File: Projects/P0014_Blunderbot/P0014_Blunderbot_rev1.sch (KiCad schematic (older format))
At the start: 6 parts

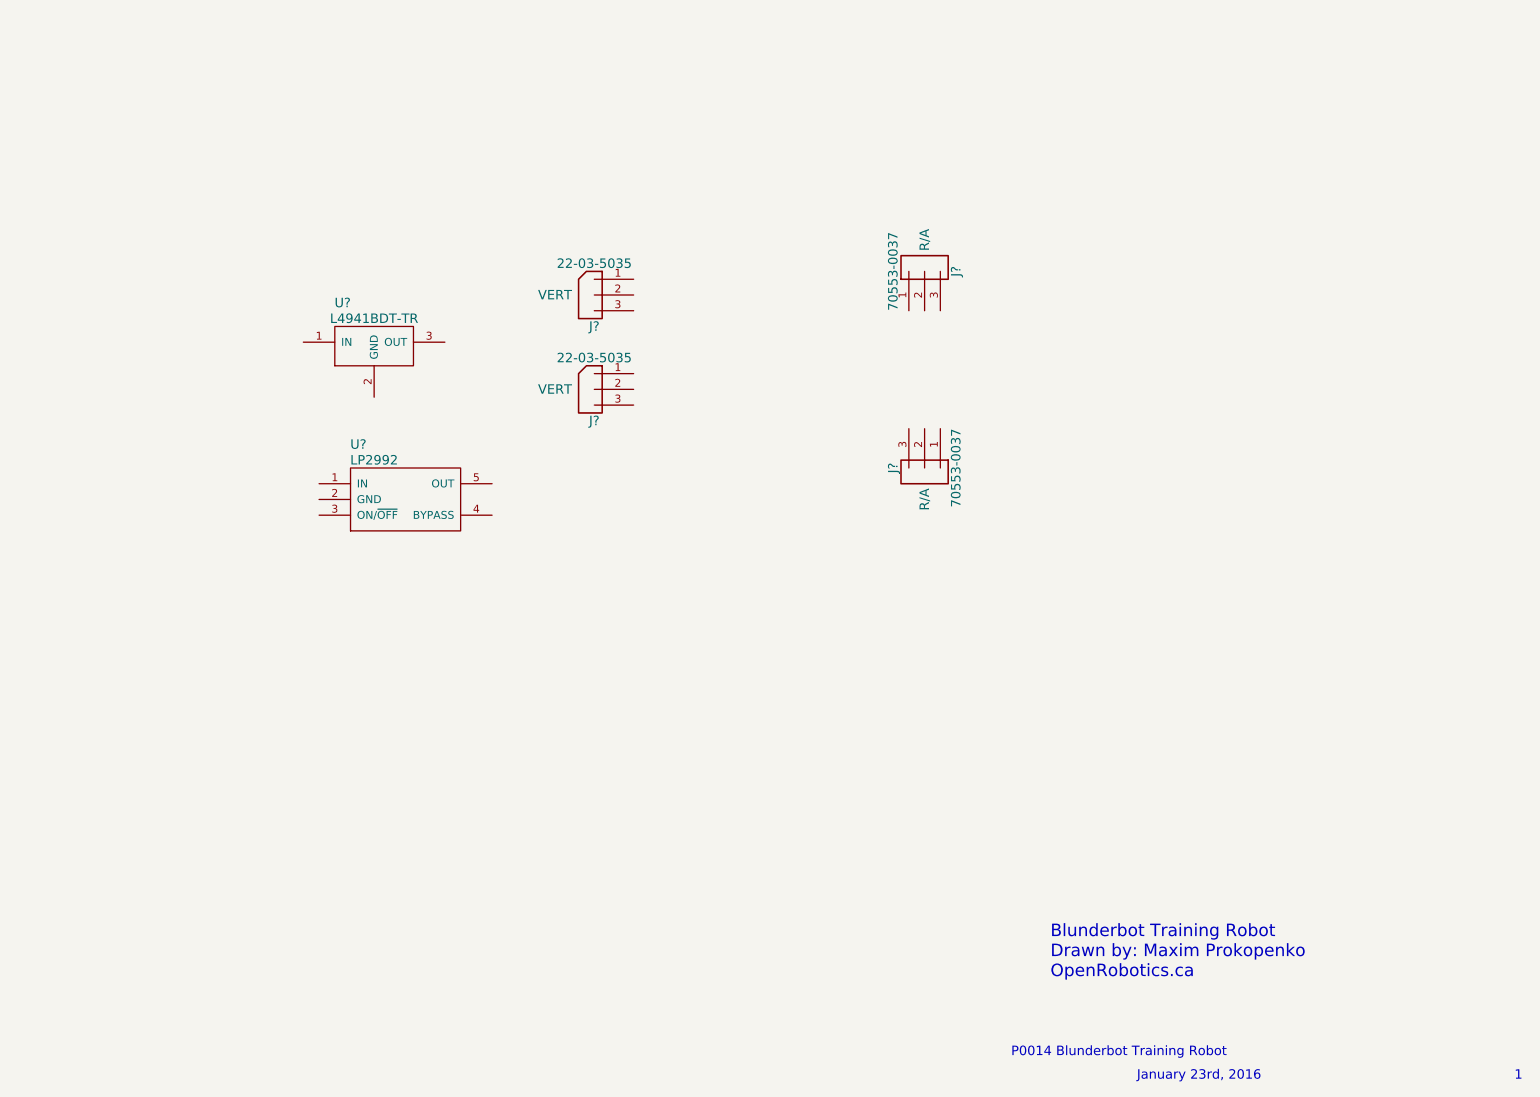
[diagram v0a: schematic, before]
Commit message: First pass at P0014rev1 schematic
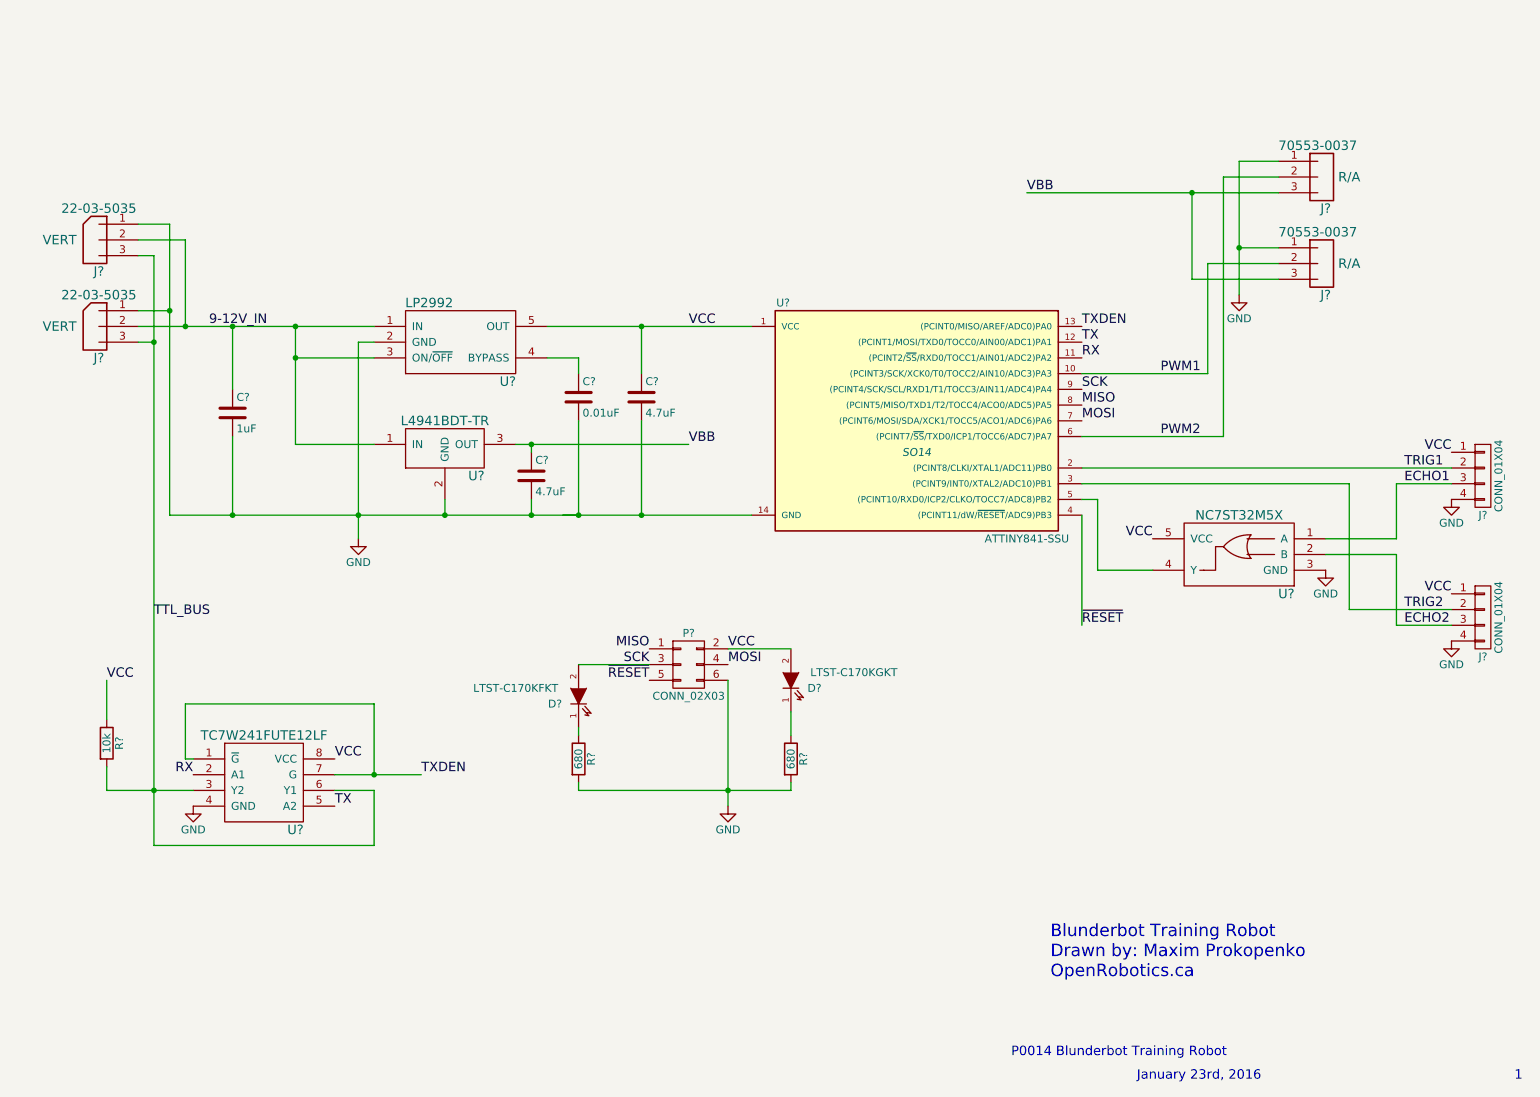
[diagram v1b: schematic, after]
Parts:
- added C?: 1uF, symbol C
- added C? (x2): 4.7uF, symbol C
- added C?: 0.01uF, symbol C
- added D?: LTST-C170KGKT, symbol LTST-C170KGKT
- added D?: LTST-C170KFKT, symbol LTST-C170KFKT
- added J? (x2): CONN_01X04, symbol CONN_01X04
- added P?: CONN_02X03, symbol CONN_02X03
- added R? (x2): 680, symbol R
- added R?: 10k, symbol R
- added U?: ATTINY841-SSU, SO14, symbol ATTINY841-SSU
- added U?: TC7W241FUTE12LF, symbol TC7W241FUTE12LF
- added U?: NC7ST32M5X, symbol NC7ST32
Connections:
- net GND: now reaches J?.1
- net GND: now also J?.1, J?.1, J?.1, U?.2 (GND), U?.2 (GND), C?.2, C?.2, C?.2, C?.2, J?.4 (P4), J?.4 (P4), P?.6 (P6), R?.2, R?.2, U?.14 (GND), U?.3 (GND), U?.4 (GND)
- net PWM1: now reaches J?.2
- net PWM1: now also U?.10 ((PCINT3/SCK/XCK0/T0/TOCC2/AIN10/ADC3)PA3)
- net VBB: now reaches J?.3
- net VBB: now also J?.3, U?.3 (OUT), C?.1
- net PWM2: now reaches J?.2
- net PWM2: now also U?.6 ((PCINT7/~SS~/TXD0/ICP1/TOCC6/ADC7)PA7)
- net 9-12V_IN: now reaches J?.2
- net 9-12V_IN: now also J?.2, U?.1 (IN), U?.1 (IN), U?.3 (ON/~OFF), C?.1
- net TTL_BUS: now reaches J?.3
- net TTL_BUS: now also J?.3, R?.2, U?.3 (Y2), U?.6 (Y1)
- net at U?.4 (BYPASS): now also C?.1
- net VCC: now reaches U?.5 (OUT)
- net VCC: now also C?.1, D?.2 (A), J?.1 (P1), J?.1 (P1), P?.2 (P2), R?.1, U?.1 (VCC), U?.5 (VCC), U?.8 (VCC)
- new net: U?.4 (Y), U?.5 ((PCINT10/RXD0/ICP2/CLKO/TOCC7/ADC8)PB2)
- new net: D?.1 (K), R?.1 (x2)
- new net ECHO1: J?.3 (P3), U?.1 (A)
- new net ECHO2: J?.3 (P3), U?.2 (B)
- new net MISO: P?.1 (P1), U?.8 ((PCINT5/MISO/TXD1/T2/TOCC4/ACO0/ADC5)PA5)
- new net MOSI: P?.4 (P4), U?.7 ((PCINT6/MOSI/SDA/XCK1/TOCC5/ACO1/ADC6)PA6)
- new net RX: U?.11 ((PCINT2/~SS~/RXD0/TOCC1/AIN01/ADC2)PA2), U?.2 (A1)
- new net SCK: D?.2 (A), P?.3 (P3), U?.9 ((PCINT4/SCK/SCL/RXD1/T1/TOCC3/AIN11/ADC4)PA4)
- new net TRIG1: J?.2 (P2), U?.2 ((PCINT8/CLKI/XTAL1/ADC11)PB0)
- new net TRIG2: J?.2 (P2), U?.3 ((PCINT9/INT0/XTAL2/ADC10)PB1)
- new net TX: U?.12 ((PCINT1/MOSI/TXD0/TOCC0/AIN00/ADC1)PA1), U?.5 (A2)
- new net TXDEN: U?.1 (~G), U?.13 ((PCINT0/MISO/AREF/ADC0)PA0), U?.7 (G)
- new net ~RESET: P?.5 (P5), U?.4 ((PCINT11/dW/~RESET~/ADC9)PB3)
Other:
- moved on the sheet: J?, U?

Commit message: Started power distribution unit
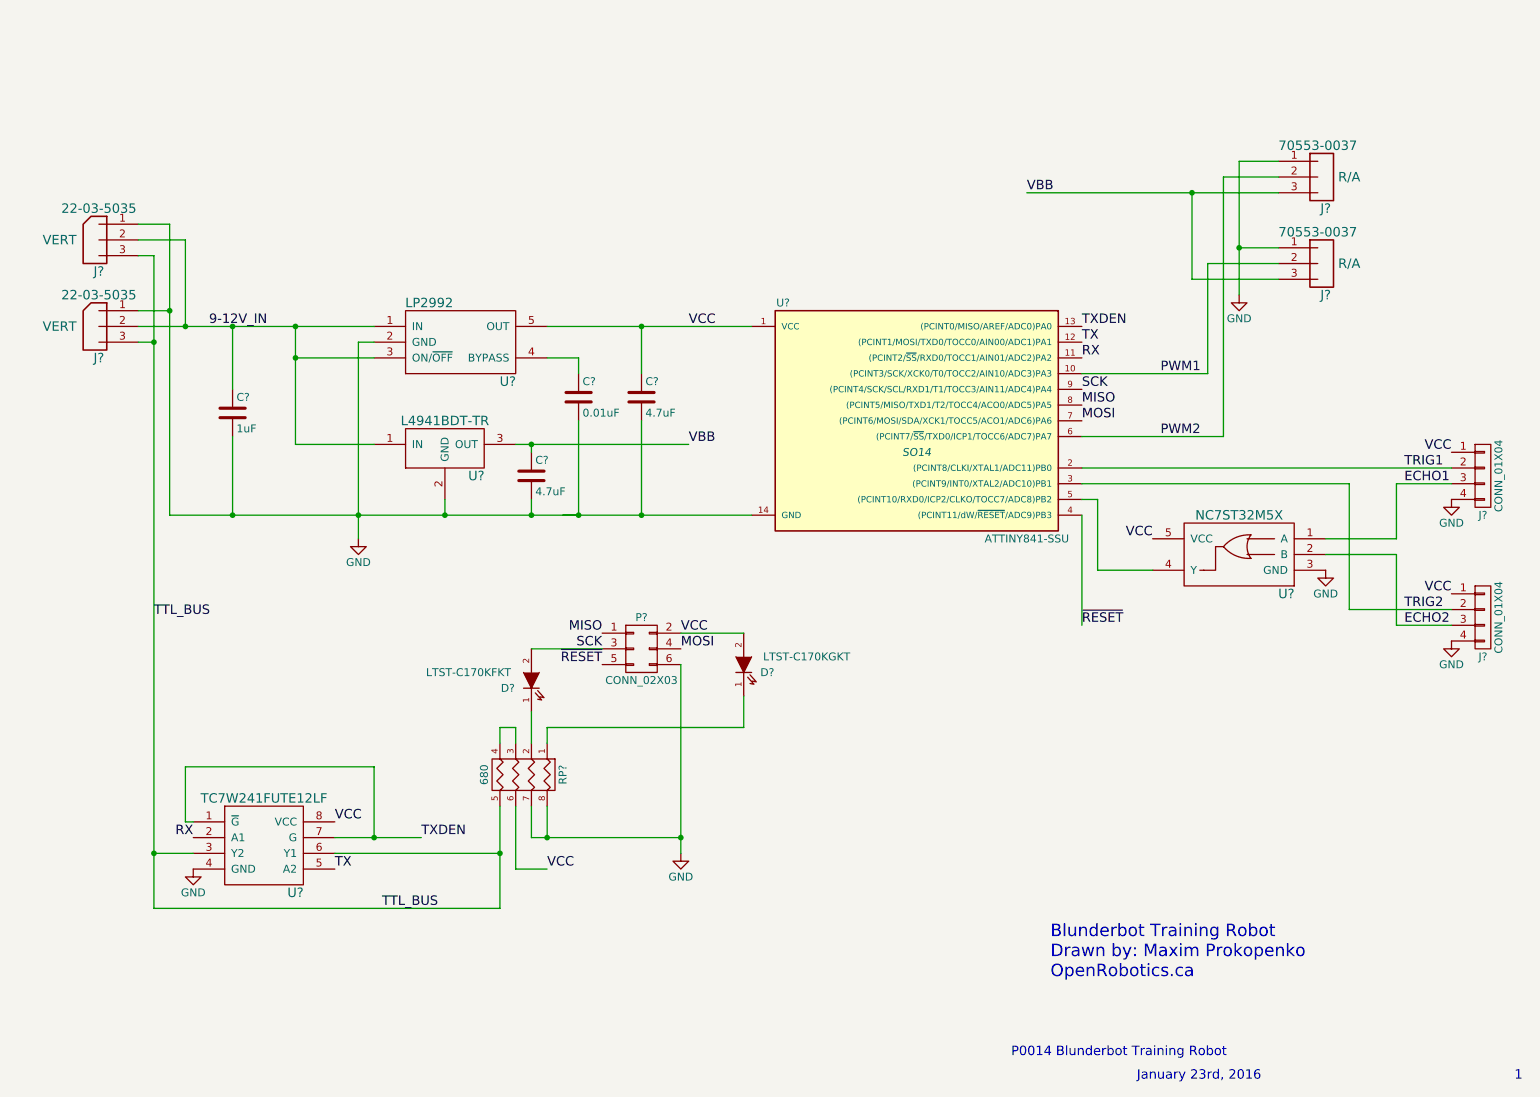
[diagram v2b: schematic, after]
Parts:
- removed R? (x2): 680, symbol R
- removed R?: 10k, symbol R
- added RP?: 680, symbol R_PACK4
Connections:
- net GND: now also RP?.7 (R2), RP?.8 (R1)
- net TTL_BUS: now also RP?.5 (R4)
- net VCC: now also RP?.6 (R3)
- net at D?.1 (K): now also RP?.1 (P1)
- net at D?.1 (K): now also RP?.2 (P2)
- new net: RP?.3 (P3), RP?.4 (P4)
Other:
- moved on the sheet: D?, P?, U?

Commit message: Layout pt 1
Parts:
- removed U?: LP2992, symbol LP2992
- removed U?: L4941BDT-TR, symbol L4941BDT-TR
- removed U?: NC7ST32M5X, symbol NC7ST32
- added C3: 470pF, Capacitors_SMD:C_0805_HandSoldering, symbol C
- added U2, U3: MIC5219-5.0YM5-TR, TO_SOT_Packages_SMD:SOT-23-5, symbol MIC5219-5.0YM5-TR
- C1, C4, C5: renamed from C?; footprint (none) -> Capacitors_SMD:C_0805_HandSoldering
- C2: renamed from C?; value 0.01uF -> 470pF; footprint (none) -> Capacitors_SMD:C_0805_HandSoldering
- D1, D2: renamed from D?; footprint (none) -> LEDs:LED_0805
- J1, J2: renamed from J?; footprint (none) -> Pin_Headers:Pin_Header_Straight_1x03
- J3, J4: renamed from J?; footprint (none) -> Pin_Headers:Pin_Header_Angled_1x03
- J5, J6: renamed from J?; footprint (none) -> Pin_Headers:Pin_Header_Straight_1x04
- P1: renamed from P?; footprint (none) -> Pin_Headers:Pin_Header_Straight_2x03
- RP1: renamed from RP?; footprint (none) -> Resistors_SMD:R_Array_Convex_4x1206
- U1: renamed from U?; footprint (none) -> Housings_SSOP:MSOP-8_3x3mm_Pitch0.65mm
- U4: renamed from U?; footprint SO14 -> SMD_Packages:SOIC-14_N
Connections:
- net TX is gone; now on net PWM1: U1.5 (A2), U4.12 ((PCINT1/MOSI/TXD0/TOCC0/AIN00/ADC1)PA1)
- net 9-12V_IN: now also U2.1 (IN), U2.3 (ON/~OFF), U3.1 (IN)
- net ECHO1: now also J5.2 (P2), U4.2 ((PCINT8/CLKI/XTAL1/ADC11)PB0); no longer J5.3 (P3)
- net ECHO2: now also J6.2 (P2), U4.5 ((PCINT10/RXD0/ICP2/CLKO/TOCC7/ADC8)PB2); no longer J6.3 (P3)
- net GND: now also J5.1 (P1), J6.1 (P1), C3.2, U2.2 (GND), U3.2 (GND); no longer J5.4 (P4), J6.4 (P4)
- net MISO: now also J3.2
- net PWM1: no longer U4.10 ((PCINT3/SCK/XCK0/T0/TOCC2/AIN10/ADC3)PA3)
- net TRIG1: now also J5.3 (P3), U4.6 ((PCINT7/~SS~/TXD0/ICP1/TOCC6/ADC7)PA7); no longer J5.2 (P2), U4.2 ((PCINT8/CLKI/XTAL1/ADC11)PB0)
- net TRIG2: now also J6.3 (P3); no longer J6.2 (P2)
- net VBB: now also U3.5 (OUT)
- net VCC: now also J5.4 (P4), J6.4 (P4), U2.5 (OUT); no longer J5.1 (P1), J6.1 (P1)
- net at C2.1: now also U3.4 (BYPASS)
- removed net PWM2: J3.2, U4.6 ((PCINT7/~SS~/TXD0/ICP1/TOCC6/ADC7)PA7)
- new net: C3.1, U2.4 (BYPASS)
- new net SERVO_EN: U3.3 (ON/~OFF), U4.10 ((PCINT3/SCK/XCK0/T0/TOCC2/AIN10/ADC3)PA3)
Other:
- moved on the sheet: C1, C2, C4, C5, D1, D2, J1, J2, J5, J6, P1, RP1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

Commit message: layout nearly done
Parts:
- added S1: MHSS1105, Pin_Headers:Pin_Header_Straight_1x03, symbol MHSS1105
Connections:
- net SERVO_EN: now also U4.13 ((PCINT0/MISO/AREF/ADC0)PA0); no longer U4.10 ((PCINT3/SCK/XCK0/T0/TOCC2/AIN10/ADC3)PA3)
- net TXDEN: now also U4.10 ((PCINT3/SCK/XCK0/T0/TOCC2/AIN10/ADC3)PA3); no longer U4.13 ((PCINT0/MISO/AREF/ADC0)PA0)
- net 9-12V_IN renamed 9-10V_IN
- net 9-10V_IN: now also S1.2; no longer U2.3 (ON/~OFF)
- net MISO renamed MISO/PWM1
- net MISO/PWM1: now also J4.2; no longer J3.2
- net MOSI renamed MOSI/PWM2
- net MOSI/PWM2: now also J3.2
- net PWM1 renamed TX
- net TX: no longer J4.2
- new net: S1.3, U2.3 (ON/~OFF)
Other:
- moved on the sheet: D2
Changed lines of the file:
@@
 	1950 2300 1950 2850
 Connection ~ 1950 2850
-Text Label 2100 2850 0    60   ~ 0
-9-12V_IN
+Text Label 1950 2300 0    60   ~ 0
+9-10V_IN
 Wire Wire Line
 	1650 2400 1750 2400
@@
 Wire Wire Line
 	1750 2950 1650 2950
-Wire Wire Line
-	3150 3050 2650 3050
 Wire Wire Line
 	2650 2850 2650 3450
@@
 Wire Wire Line
 	2650 3450 3150 3450
-Connection ~ 2650 3050
 Wire Wire Line
 	3150 2950 2850 2950
@@
 Connection ~ 1850 2750
 Wire Wire Line
-	2250 3250 2250 2850
+	2250 2550 2250 3250
 Connection ~ 2250 2850
 Wire Wire Line
@@
 Text Label 7800 4750 0    60   ~ 0
 ~RESET
-Text Label 7800 3350 0    60   ~ 0
-MISO
 Text Label 7800 3450 0    60   ~ 0
-MOSI
+MOSI/PWM2
 Text Label 7800 3250 0    60   ~ 0
 SCK
@@
 RX
 Wire Wire Line
-	8600 2950 8600 2450
-Wire Wire Line
 	8600 2450 9050 2450
-Text Label 8300 2950 0    60   ~ 0
-PWM1
 Wire Wire Line
 	9050 2350 8800 2350
@@
 	1    0    0    -1
 $EndComp
-Text Label 9300 3550 0    60   ~ 0
+Text Label 7800 3550 0    60   ~ 0
 TRIG1
-Text Label 9300 4200 0    60   ~ 0
+Text Label 7800 3850 0    60   ~ 0
 TRIG2
-Text Label 9300 4300 0    60   ~ 0
+Text Label 7800 3950 0    60   ~ 0
 ECHO2
-Text Label 7800 2850 0    60   ~ 0
+Text Label 7800 3150 0    60   ~ 0
 TXDEN
 $Comp
 L LTST-C170KGKT D2
 U 1 1 56A60844
-P 5550 5000
-F 0 "D2" V 5500 4850 50  0000 C CNN
-F 1 "LTST-C170KGKT" V 5600 4600 50  0000 C CNN
-F 2 "LEDs:LED_0805" V 5550 5000 50  0001 C CNN
-F 3 "" H 5550 5000 50  0000 C CNN
-	1    5550 5000
+P 5850 5000
+F 0 "D2" V 5800 4850 50  0000 C CNN
+F 1 "LTST-C170KGKT" V 5900 4600 50  0000 C CNN
+F 2 "LEDs:LED_0805" V 5850 5000 50  0001 C CNN
+F 3 "" H 5850 5000 50  0000 C CNN
+	1    5850 5000
 	0    -1   -1   0
 $EndComp
@@
 $EndComp
 Wire Wire Line
-	5100 4800 5550 4800
+	5100 4800 5850 4800
 Text Label 4600 4800 2    60   ~ 0
-MISO
+MISO/PWM1
 Text Label 4600 4900 2    60   ~ 0
 SCK
@@
 VCC
 Text Label 5100 4900 0    60   ~ 0
-MOSI
-Wire Wire Line
-	5550 5200 5550 5400
+MOSI/PWM2
+Wire Wire Line
+	5850 5200 5850 5400
 Wire Wire Line
 	4150 5300 4150 5500
@@
 	4250 5500 4250 5400
 Wire Wire Line
-	4250 5400 5550 5400
+	4250 5400 5850 5400
 Wire Wire Line
 	4250 5900 4250 6100
@@
 	9050 1900 8950 1900
 Wire Wire Line
-	8950 1900 8950 3350
-Wire Wire Line
-	8950 3350 7800 3350
-Text Label 8300 3350 0    60   ~ 0
-PWM2
-Wire Wire Line
-	8600 2950 7800 2950
+	8950 1900 8950 3450
+Text Label 7800 3350 0    60   ~ 0
+MISO/PWM1
 Wire Wire Line
 	9600 3550 7800 3550
@@
 	8700 3650 8700 3750
 Wire Wire Line
-	8700 3750 7800 3750
-Wire Wire Line
 	7800 3850 8700 3850
 Wire Wire Line
@@
 Wire Wire Line
 	8600 3950 7800 3950
-Text Label 9300 3650 0    60   ~ 0
+Text Label 7800 3750 0    60   ~ 0
 ECHO1
+$Comp
+L MIC5219-5.0YM5-TR U3
+U 1 1 56C97863
+P 3700 3450
+F 0 "U3" H 4000 3100 60  0000 C CNN
+F 1 "MIC5219-5.0YM5-TR" H 3700 3600 60  0000 C CNN
+F 2 "TO_SOT_Packages_SMD:SOT-23-5" H 3700 3450 60  0001 C CNN
+F 3 "" H 3700 3450 60  0000 C CNN
+	1    3700 3450
+	1    0    0    -1
+$EndComp
+Wire Wire Line
+	3150 3550 2950 3550
+Wire Wire Line
+	2950 3550 2950 4050
+Connection ~ 2950 4050
+Text Label 7800 2850 0    60   ~ 0
+SERVO_EN
+Text Label 3050 4500 0    60   ~ 0
+SERVO_EN
+Wire Wire Line
+	3050 4500 3050 3650
+Wire Wire Line
+	3050 3650 3150 3650
+Wire Wire Line
+	4250 3650 4400 3650
+Wire Wire Line
+	4400 3650 4400 3700
+Wire Wire Line
+	4400 4000 4400 4050
+Connection ~ 4400 4050
+$Comp
+L C C3
+U 1 1 56C98142
+P 4700 3250
+F 0 "C3" H 4725 3350 50  0000 L CNN
+F 1 "470pF" H 4725 3150 50  0000 L CNN
+F 2 "Capacitors_SMD:C_0805_HandSoldering" H 4738 3100 50  0001 C CNN
+F 3 "" H 4700 3250 50  0000 C CNN
+	1    4700 3250
+	1    0    0    -1
+$EndComp
+Wire Wire Line
+	4700 3400 4700 4050
+Connection ~ 4700 4050
+Wire Wire Line
+	4700 3050 4700 3100
+Wire Wire Line
+	4250 3450 5000 3450
+Wire Wire Line
+	5000 2000 5000 3700
+Wire Wire Line
+	5000 4000 5000 4050
+Connection ~ 5000 4050
+Connection ~ 5000 3450
 $Comp
 L MIC5219-5.0YM5-TR U2
@@
 	1    0    0    -1
 $EndComp
-$Comp
-L MIC5219-5.0YM5-TR U3
-U 1 1 56C97863
-P 3700 3450
-F 0 "U3" H 4000 3100 60  0000 C CNN
-F 1 "MIC5219-5.0YM5-TR" H 3700 3600 60  0000 C CNN
-F 2 "TO_SOT_Packages_SMD:SOT-23-5" H 3700 3450 60  0001 C CNN
-F 3 "" H 3700 3450 60  0000 C CNN
-	1    3700 3450
-	1    0    0    -1
-$EndComp
-Wire Wire Line
-	3150 3550 2950 3550
-Wire Wire Line
-	2950 3550 2950 4050
-Connection ~ 2950 4050
-Wire Wire Line
-	7800 3150 8300 3150
-Text Label 8300 3150 0    60   ~ 0
-SERVO_EN
-Text Label 3050 4500 0    60   ~ 0
-SERVO_EN
-Wire Wire Line
-	3050 4500 3050 3650
-Wire Wire Line
-	3050 3650 3150 3650
-Wire Wire Line
-	4250 3650 4400 3650
-Wire Wire Line
-	4400 3650 4400 3700
-Wire Wire Line
-	4400 4000 4400 4050
-Connection ~ 4400 4050
-$Comp
-L C C3
-U 1 1 56C98142
-P 4700 3250
-F 0 "C3" H 4725 3350 50  0000 L CNN
-F 1 "470pF" H 4725 3150 50  0000 L CNN
-F 2 "Capacitors_SMD:C_0805_HandSoldering" H 4738 3100 50  0001 C CNN
-F 3 "" H 4700 3250 50  0000 C CNN
-	1    4700 3250
-	1    0    0    -1
-$EndComp
-Wire Wire Line
-	4700 3400 4700 4050
-Connection ~ 4700 4050
-Wire Wire Line
-	4700 3050 4700 3100
-Wire Wire Line
-	4250 3450 5000 3450
-Wire Wire Line
-	5000 2000 5000 3700
-Wire Wire Line
-	5000 4000 5000 4050
-Connection ~ 5000 4050
-Connection ~ 5000 3450
+Wire Wire Line
+	8700 3750 7800 3750
+$Comp
+L MHSS1105 S1
+U 1 1 56C9F259
+P 2750 2550
+F 0 "S1" H 2950 2375 60  0000 C CNN
+F 1 "MHSS1105" H 2750 2775 60  0000 C CNN
+F 2 "Pin_Headers:Pin_Header_Straight_1x03" H 2860 2550 60  0001 C CNN
+F 3 "" H 2860 2550 60  0000 C CNN
+	1    2750 2550
+	1    0    0    -1
+$EndComp
+Wire Wire Line
+	3050 2650 3100 2650
+Wire Wire Line
+	3100 2650 3100 3050
+Wire Wire Line
+	3100 3050 3150 3050
+Wire Wire Line
+	2450 2550 2250 2550
+Wire Wire Line
+	8600 2450 8600 3350
+Wire Wire Line
+	8600 3350 7800 3350
+Wire Wire Line
+	8950 3450 7800 3450
 $EndSCHEMATC
